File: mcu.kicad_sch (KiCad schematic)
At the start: 38 parts, among them J3 Conn_ST_STDC14, J4 USB_5V, J5 E5V, SW2 BOOT0 pull, U1 STM32G474RETx, U2 AMS1117-3.3, Y1 Crystal 32.768KHz, Y2 Crystal 24MHz

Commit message: Added finishing thouches to brake sense pcb Finished main schematic layout and added chosen component footprints Placed components in layout and started tracing
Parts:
- removed C43, C50: 100nF, Capacitor_SMD:C_0603_1608Metric_Pad1.08x0.95mm_HandSolder, symbol Device:C
- removed J4: USB_5V, Project_Footprints:HARWIN_M20-9990246, symbol M20-9990246:M20-9990246
- removed J5: E5V, Project_Footprints:HARWIN_M20-9990246, symbol M20-9990246:M20-9990246
- removed R27: 47, Resistor_SMD:R_0805_2012Metric_Pad1.20x1.40mm_HandSolder, symbol Device:R
- removed U2: AMS1117-3.3, Package_TO_SOT_SMD:SOT-223-3_TabPin2, symbol Regulator_Linear:AMS1117-3.3
- added C31, C33: 100nF, Capacitor_SMD:C_0603_1608Metric, symbol Device:C
- added C32: 1μF, Capacitor_SMD:C_0603_1608Metric, symbol Device:C
- added D4: APT2012CGCK, LED_SMD:LED_0805_2012Metric, symbol Device:LED
- added D5, D6: SS34, Diode_SMD:D_SOD-323, symbol Device:D_Zener
- added FB2: 600R@100MHz, Inductor_SMD:L_0603_1608Metric, symbol Device:FerriteBead
- added J3: USB_5V, tinynav:HARWIN_M20-9990246, symbol tinynav:M20-9990246
- added J4: E5V, tinynav:HARWIN_M20-9990246, symbol tinynav:M20-9990246
- added J5: Curr_measure, tinynav:HARWIN_M20-9990246, symbol tinynav:M20-9990246
- added R13: 560, Resistor_SMD:R_0805_2012Metric, symbol Device:R
- added U5: TLV75533PDBV, Package_TO_SOT_SMD:SOT-23-5, symbol Regulator_Linear:TLV75533PDBV
- C12: renamed from C8; value 22u -> 1μF; footprint Capacitor_SMD:C_0805_2012Metric -> Capacitor_SMD:C_0603_1608Metric
- C13: renamed from C77; footprint Capacitor_SMD:C_0603_1608Metric_Pad1.08x0.95mm_HandSolder -> Capacitor_SMD:C_0603_1608Metric
- C20: renamed from C40; footprint Capacitor_SMD:C_1206_3216Metric_Pad1.33x1.80mm_HandSolder -> Capacitor_SMD:C_1206_3216Metric
- C21: renamed from C44; footprint Capacitor_SMD:C_0603_1608Metric_Pad1.08x0.95mm_HandSolder -> Capacitor_SMD:C_0603_1608Metric
- C22: renamed from C47; footprint Capacitor_SMD:C_0603_1608Metric_Pad1.08x0.95mm_HandSolder -> Capacitor_SMD:C_0603_1608Metric
- C23: renamed from C48; footprint Capacitor_SMD:C_0603_1608Metric_Pad1.08x0.95mm_HandSolder -> Capacitor_SMD:C_0603_1608Metric
- C24: renamed from C49; footprint Capacitor_SMD:C_0603_1608Metric_Pad1.08x0.95mm_HandSolder -> Capacitor_SMD:C_0603_1608Metric
- C26: renamed from C41; footprint Capacitor_SMD:C_0805_2012Metric_Pad1.18x1.45mm_HandSolder -> Capacitor_SMD:C_0603_1608Metric
- C27: renamed from C45; footprint Capacitor_SMD:C_0603_1608Metric_Pad1.08x0.95mm_HandSolder -> Capacitor_SMD:C_0603_1608Metric
- C28: renamed from C42; footprint Capacitor_SMD:C_0805_2012Metric_Pad1.18x1.45mm_HandSolder -> Capacitor_SMD:C_0603_1608Metric
- C29: renamed from C46; footprint Capacitor_SMD:C_0603_1608Metric_Pad1.08x0.95mm_HandSolder -> Capacitor_SMD:C_0603_1608Metric
- C30: renamed from C76; footprint Capacitor_SMD:C_0603_1608Metric_Pad1.08x0.95mm_HandSolder -> Capacitor_SMD:C_0603_1608Metric
- R10: renamed from R24; footprint Resistor_SMD:R_0805_2012Metric_Pad1.20x1.40mm_HandSolder -> Resistor_SMD:R_0805_2012Metric
- R11: renamed from R25; footprint Resistor_SMD:R_0805_2012Metric_Pad1.20x1.40mm_HandSolder -> Resistor_SMD:R_0805_2012Metric
- R12: renamed from R23; footprint Resistor_SMD:R_0805_2012Metric_Pad1.20x1.40mm_HandSolder -> Resistor_SMD:R_0805_2012Metric
- Y1: renamed from Y2; footprint Crystal:Crystal_SMD_3225-4Pin_3.2x2.5mm -> Crystal:Crystal_SMD_2016-4Pin_2.0x1.6mm
- renumbered C3 to C10, C4 to C11, C5 to C8, C6 to C9, J3 to J2, R2 to R5, R1 to R6, R3 to R7, R4 to R8, R5 to R9, Y1 to Y2
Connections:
- net +3V3: now also U1.1 (VBAT), U1.16 (VDD), U1.32 (VDD), U1.48 (VDD), U1.64 (VDD), C33.1, FB2.1, J5.1; no longer C12.1, C26.1, C27.1, C28.1, C29.1
- net E5V: now also J4.2
- net GND: now also C12.2, R7.2, C31.2, C32.2, C33.2, D4.1 (K), U5.2 (GND)
- net USB/USB_5V: now also J3.2
- net SWDIO: now reaches R10.2, U1.49 (PA13)
- net HSE_OUT: now reaches C9.2, U1.6 (PF1), Y1.3
- net NRST: now reaches C13.1, D11.1 (K), J2.12 (~{RST}), RESET1.1 (A), U1.7 (PG10)
- net LSE_IN: now reaches R6.2, U1.3 (PC14)
- net HSE_IN: now reaches R5.2, U1.5 (PF0)
- net LSE_OUT: now reaches C11.2, U1.4 (PC15), Y2.2
- net BOOT: now reaches R12.1, U1.61 (PB8)
- net SWCLK: now reaches R11.2, U1.50 (PA14)
- new net: D4.2 (A), R13.2
- new net: D6.2 (A), J4.1
- new net: D5.2 (A), J3.1
- new net +5V: C31.1, C32.1, D5.1 (K), D6.1 (K), R13.1, U5.1 (IN), U5.3 (EN)
- new net 3.3V_OUT: C12.1, J5.2, U5.5 (OUT)
- new net VDDA: C26.1, C27.1, C28.1, C29.1, FB2.2, U1.28 (VREF+), U1.29 (VDDA)
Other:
- note added: "Don't need both mechanical (jumper) and diode protection Using both to test if one work better"
- note added: "VDDA/ VREF+"
- note removed: "BOOT"
- note removed: "NRST"
- note removed: "VDDA"
- moved on the sheet: C12, C13, C20, C21, C22, C23, C24, C26, C27, C28, C29, C30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

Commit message: Added Current reading for INA228 Started rev 02 on brake sense
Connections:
- net +3V3: now also R8.2, R9.2
- net GND: no longer R8.2, R9.2
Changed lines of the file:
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@@
 	)
 	(junction
+		(at 92.71 152.4)
+		(diameter 0)
+		(color 0 0 0 0)
+	)
+	(junction
 		(at 54.61 179.07)
 		(diameter 0)
@@
 	)
 	(junction
-		(at 92.71 152.4)
-		(diameter 0)
-		(color 0 0 0 0)
-	)
-	(junction
 		(at 262.89 130.81)
 		(diameter 0)
@@
 	(wire
 		(pts
-			(xy 92.71 152.4) (xy 96.52 152.4)
+			(xy 88.9 152.4) (xy 92.71 152.4)
 		)
 		(stroke
@@
 	(wire
 		(pts
-			(xy 88.9 152.4) (xy 92.71 152.4)
-		)
-		(stroke
-			(width 0)
-			(type default)
-		)
-	)
-	(wire
-		(pts
 			(xy 78.74 50.8) (xy 78.74 49.53)
 		)
@@
 	(wire
 		(pts
+			(xy 92.71 152.4) (xy 96.52 152.4)
+		)
+		(stroke
+			(width 0)
+			(type default)
+		)
+	)
+	(wire
+		(pts
 			(xy 90.17 33.02) (xy 90.17 38.1)
 		)
@@
 	)
 	(symbol
+		(lib_id "power:+3V3")
+		(at 92.71 152.4 180)
+		(unit 1)
+		(body_style 1)
+		(exclude_from_sim no)
+		(in_bom yes)
+		(on_board yes)
+		(in_pos_files yes)
+		(dnp no)
+		(fields_autoplaced yes)
+		(property "Reference" "#PWR058"
+			(at 92.71 148.59 0)
+			(hide yes)
+			(show_name no)
+			(do_not_autoplace no)
+			(effects
+				(font
+					(size 1.27 1.27)
+				)
+			)
+		)
+		(property "Value" "+3V3"
+			(at 92.71 157.48 0)
+			(show_name no)
+			(do_not_autoplace no)
+			(effects
+				(font
+					(size 1.27 1.27)
+				)
+			)
+		)
+		(property "Footprint" ""
+			(at 92.71 152.4 0)
+			(hide yes)
+			(show_name no)
+			(do_not_autoplace no)
+			(effects
+				(font
+					(size 1.27 1.27)
+				)
+			)
+		)
+		(property "Datasheet" ""
+			(at 92.71 152.4 0)
+			(hide yes)
+			(show_name no)
+			(do_not_autoplace no)
+			(effects
+				(font
+					(size 1.27 1.27)
+				)
+			)
+		)
+		(property "Description" "Power symbol creates a global label with name \"+3V3\""
+			(at 92.71 152.4 0)
+			(hide yes)
+			(show_name no)
+			(do_not_autoplace no)
+			(effects
+				(font
+					(size 1.27 1.27)
+				)
+			)
+		)
+		(pin "1"
+		)
+		(instances
+			(project "Nucleo_devboard"
+				(path "/4250c3cc-f8c5-441a-9e80-e89bb6ada756/77213db3-d061-4eb8-a107-9e1bca2752d0"
+					(reference "#PWR058")
+					(unit 1)
+				)
+			)
+		)
+	)
+	(symbol
 		(lib_id "tinynav:M20-9990246")
 		(at 44.45 52.07 270)
@@
 					(unit 1)
 				)
-			)
-		)
-	)
-	(symbol
-		(lib_id "power:GND")
-		(at 92.71 152.4 0)
-		(unit 1)
-		(body_style 1)
-		(exclude_from_sim no)
-		(in_bom yes)
-		(on_board yes)
-		(in_pos_files yes)
-		(dnp no)
-		(fields_autoplaced yes)
-		(property "Reference" "#PWR06"
-			(at 92.71 158.75 0)
-			(hide yes)
-			(show_name no)
-			(do_not_autoplace no)
-			(effects
-				(font
-					(size 1.27 1.27)
-				)
-			)
-		)
-		(property "Value" "GND"
-			(at 92.71 157.48 0)
-			(show_name no)
-			(do_not_autoplace no)
-			(effects
-				(font
-					(size 1.27 1.27)
-				)
-			)
-		)
-		(property "Footprint" ""
-			(at 92.71 152.4 0)
-			(hide yes)
-			(show_name no)
-			(do_not_autoplace no)
-			(effects
-				(font
-					(size 1.27 1.27)
-				)
-			)
-		)
-		(property "Datasheet" ""
-			(at 92.71 152.4 0)
-			(hide yes)
-			(show_name no)
-			(do_not_autoplace no)
-			(effects
-				(font
-					(size 1.27 1.27)
-				)
-			)
-		)
-		(property "Description" "Power symbol creates a global label with name \"GND\" , ground"
-			(at 92.71 152.4 0)
-			(hide yes)
-			(show_name no)
-			(do_not_autoplace no)
-			(effects
-				(font
-					(size 1.27 1.27)
-				)
-			)
-		)
-		(pin "1"
-		)
-		(instances
-			(project "Nucleo_devboard"
-				(path "/4250c3cc-f8c5-441a-9e80-e89bb6ada756/77213db3-d061-4eb8-a107-9e1bca2752d0"
-					(reference "#PWR06")
-					(unit 1)
-				)

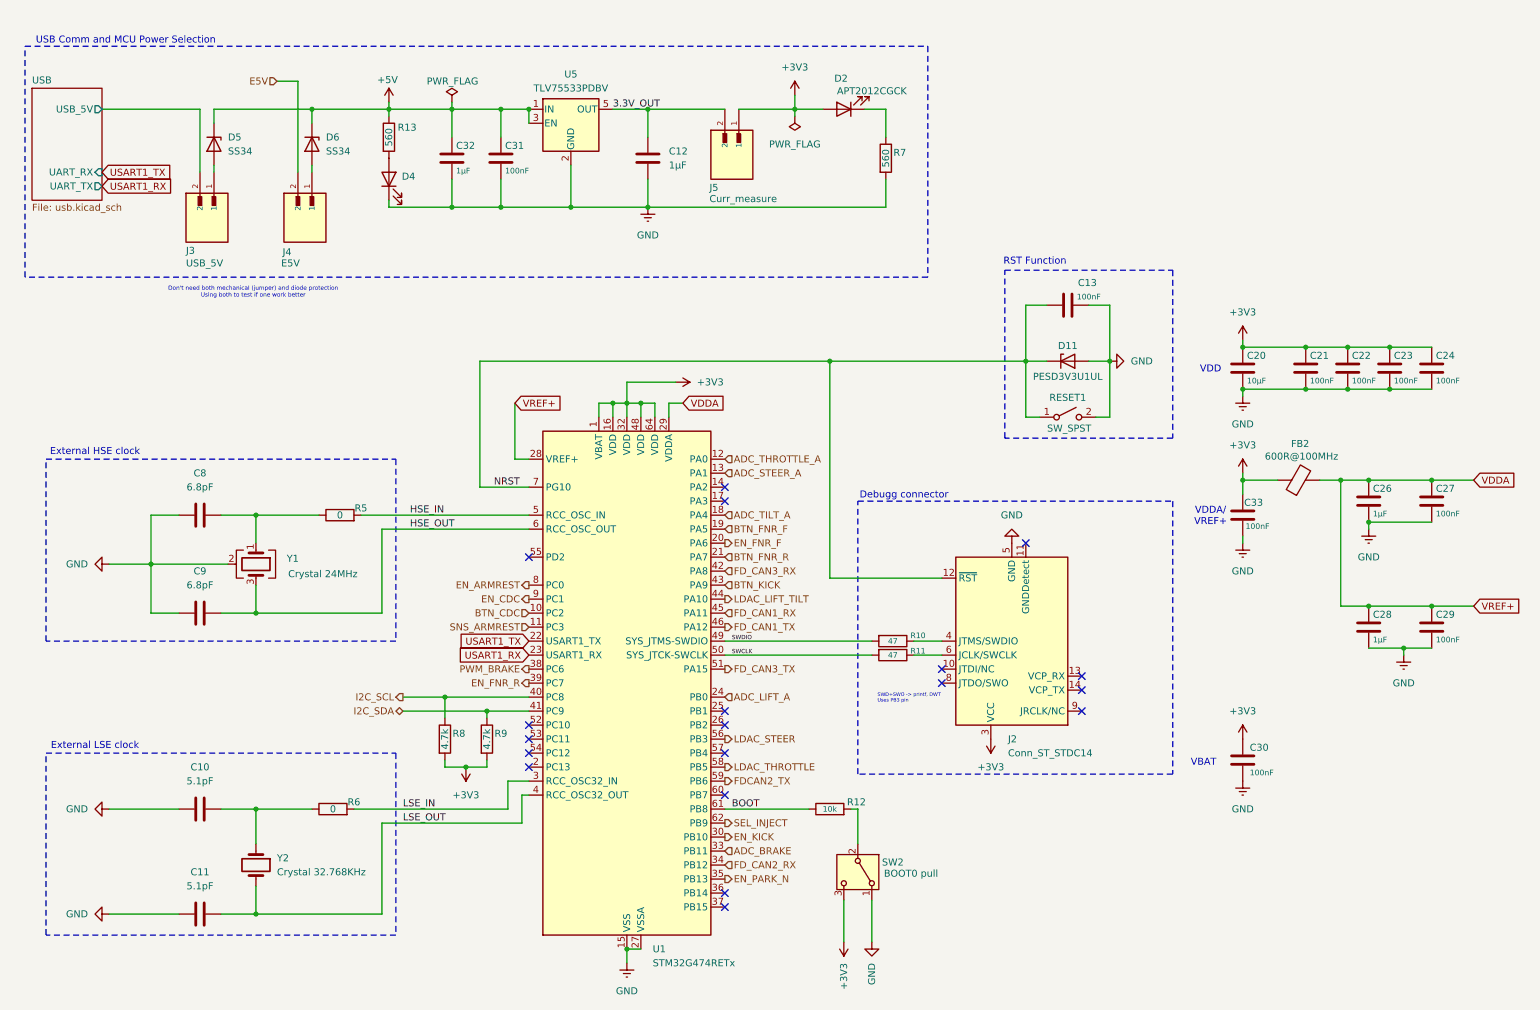
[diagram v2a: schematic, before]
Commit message: added rev04_mcu1/2.h revised brake sense board Added logic for 2 MCUs on nucleo board
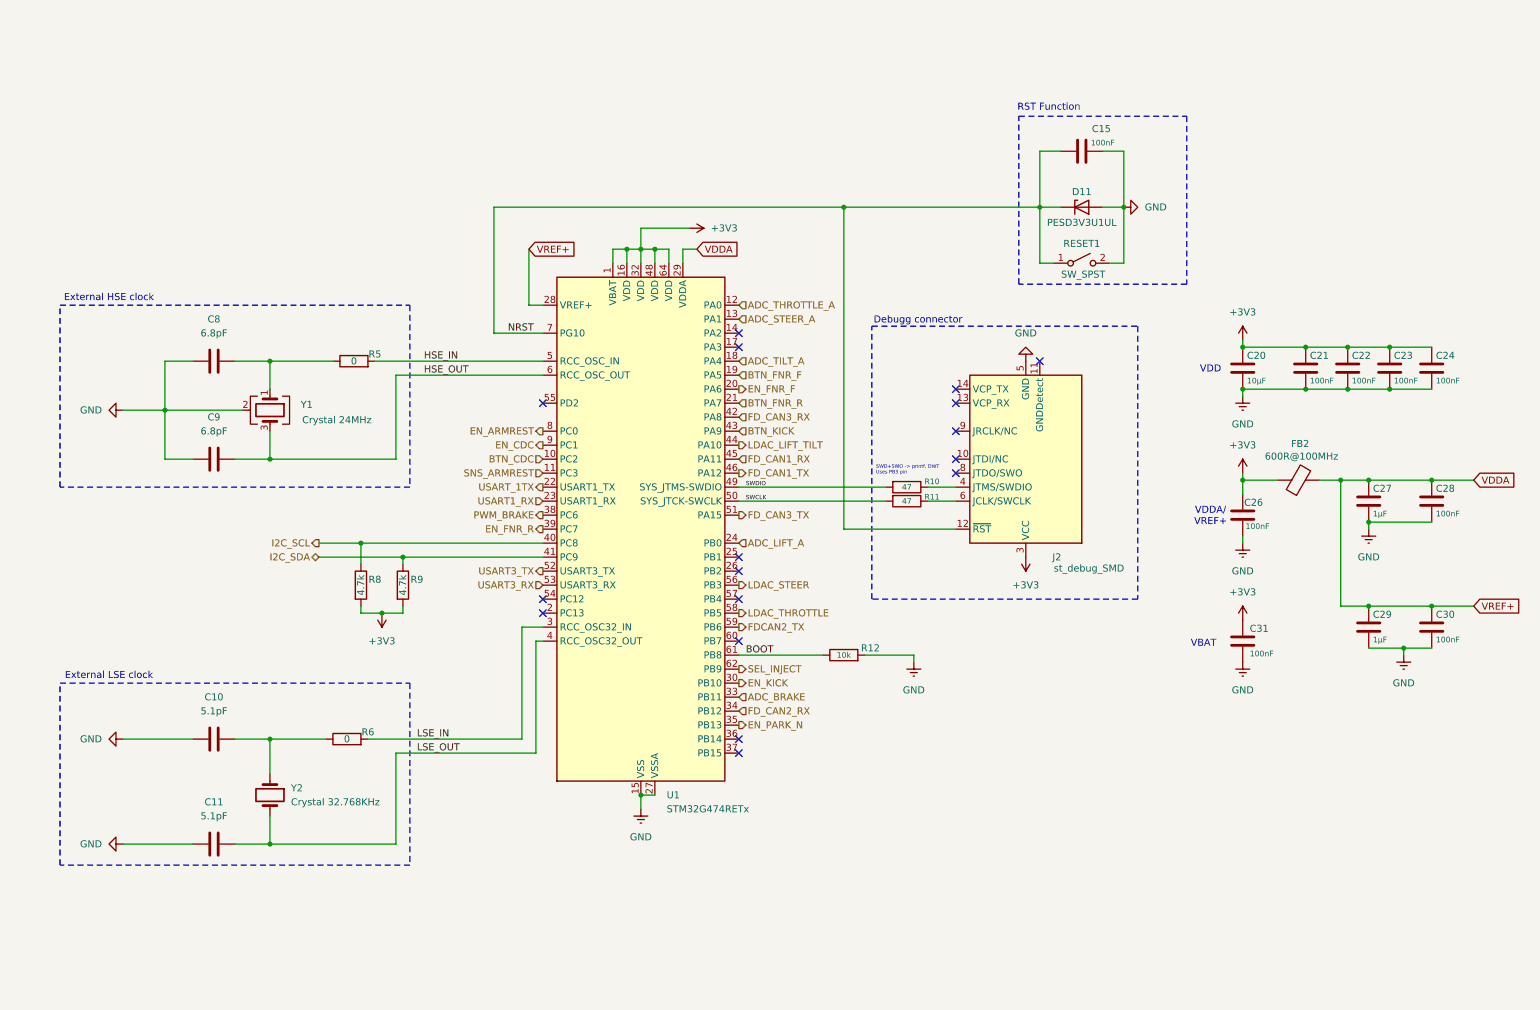
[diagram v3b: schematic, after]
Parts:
- removed C12, C32: 1μF, Capacitor_SMD:C_0603_1608Metric, symbol Device:C
- removed C31: 100nF, Capacitor_SMD:C_0603_1608Metric, symbol Device:C
- removed D2, D4: APT2012CGCK, LED_SMD:LED_0805_2012Metric, symbol Device:LED
- removed D5, D6: SS34, Diode_SMD:D_SOD-323, symbol Device:D_Zener
- removed J2: Conn_ST_STDC14, Connector_PinHeader_1.27mm:PinHeader_2x07_P1.27mm_Vertical, symbol Connector:Conn_ST_STDC14
- removed J3: USB_5V, tinynav:HARWIN_M20-9990246, symbol tinynav:M20-9990246
- removed J4: E5V, tinynav:HARWIN_M20-9990246, symbol tinynav:M20-9990246
- removed J5: Curr_measure, tinynav:HARWIN_M20-9990246, symbol tinynav:M20-9990246
- removed R13, R7: 560, Resistor_SMD:R_0805_2012Metric, symbol Device:R
- removed SW2: BOOT0 pull, Button_Switch_THT:SW_Slide_SPDT_Straight_CK_OS102011MS2Q, symbol Switch:SW_SPDT
- removed U5: TLV75533PDBV, Package_TO_SOT_SMD:SOT-23-5, symbol Regulator_Linear:TLV75533PDBV
- added J2: st_debug_SMD, tinynav:PinHeader_2x07_P1.27mm_Vertical_SMD, symbol tinynav:st_debug_SMD
- renumbered C13 to C15, C33 to C26, C26 to C27, C27 to C28, C28 to C29, C29 to C30, C30 to C31
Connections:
- net +3V3: now also J2.3 (VCC)
- net GND: now also R12.2, J2.5 (GND), J2.7 (GND)
- net NRST: now also J2.12 (~{RST})
- net at R10.1: now also J2.4 (JTMS/SWDIO)
- net at R11.1: now also J2.6 (JCLK/SWCLK)
- net USART3_TX: now reaches U1.52 (PC10)
- net USART3_RX: now reaches U1.53 (PC11)
- net USART1_TX renamed USART_1TX
- no-connect marks 19 -> 17
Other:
- removed sheet USB
- note removed: "Don't need both mechanical (jumper) and diode protection Using both to test if one work better"
- note removed: "USB Comm and MCU Power Selection"
- moved on the sheet: C10, C11, C15, C31, C8, C9, D11, R10, R11, R12, R5, R6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

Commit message: Generated scaffold for mcu2 finished brake sense rev2 finished adding second chip to nucleo devboard
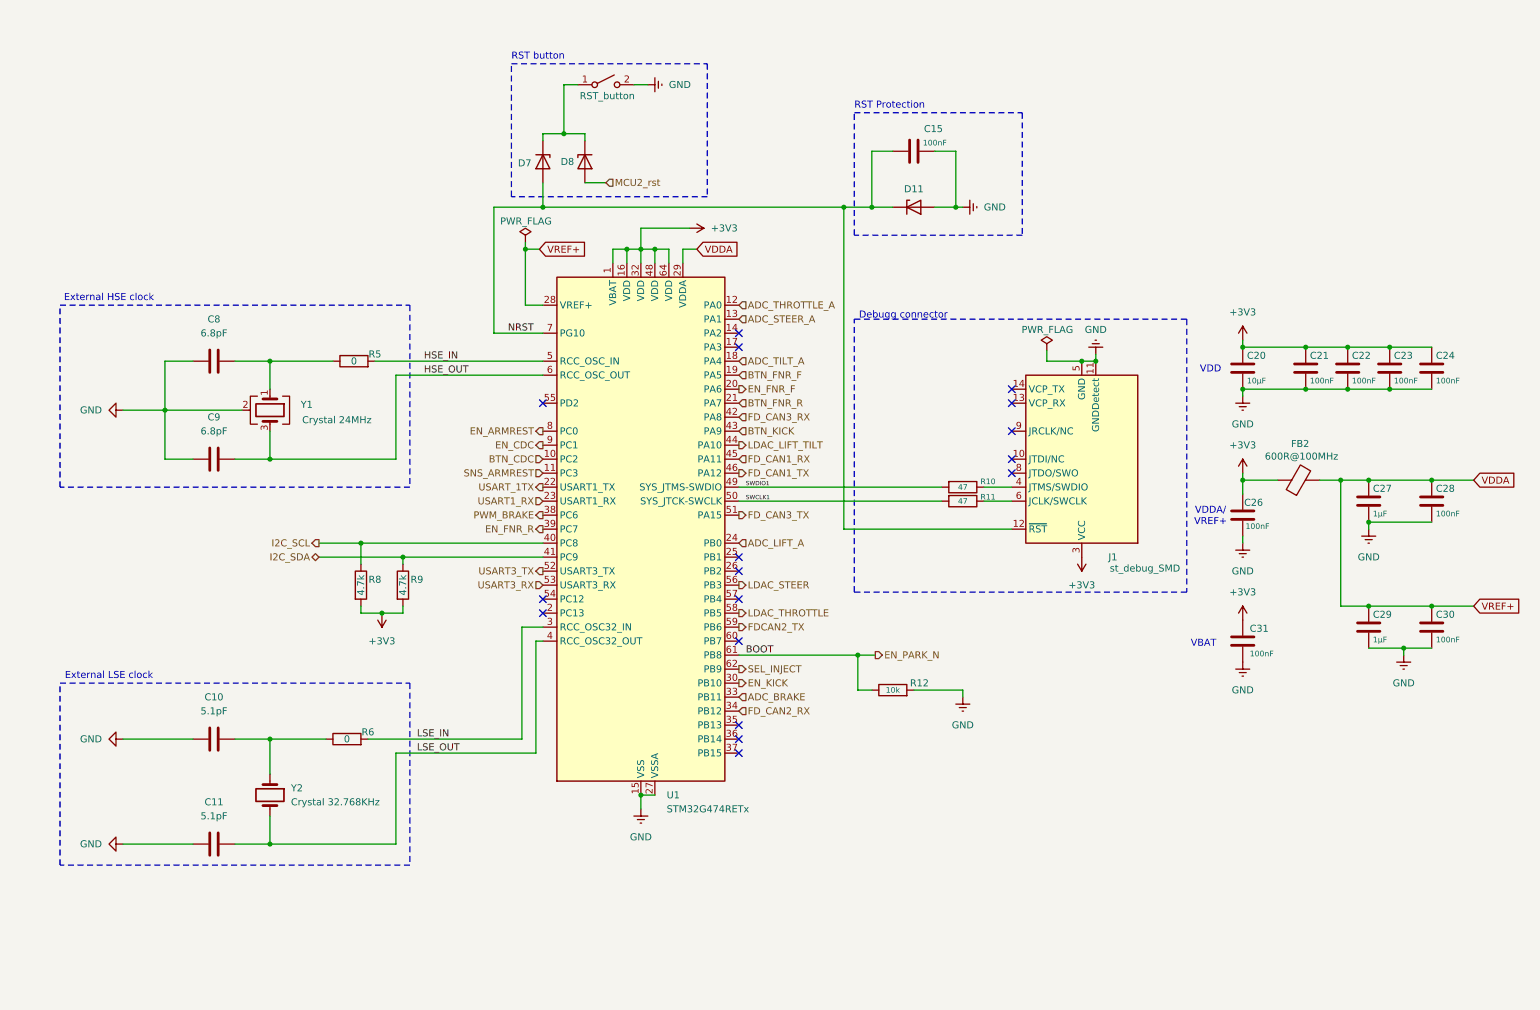
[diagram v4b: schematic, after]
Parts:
- added D7, D8: BAT60A, Diode_SMD:D_SOD-323, symbol Device:D_Zener
- D11: value PESD3V3U1UL -> CDSOD323-T03; footprint Diode_SMD:D_SOD-882 -> Diode_SMD:D_SOD-323
- RESET1: value SW_SPST -> RST_button
- renumbered J2 to J1
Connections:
- net BOOT is gone; now on net EN_PARK_N: R12.1, U1.61 (PB8)
- net EN_PARK_N: no longer U1.35 (PB13)
- net GND: now also J1.11 (GNDDetect)
- net NRST: now also D7.2 (A); no longer RESET1.1 (A)
- net SWCLK renamed SWCLK1
- net SWDIO renamed SWDIO1
- new net: D7.1 (K), D8.1 (K), RESET1.1 (A)
- new net MCU2_rst: D8.2 (A)
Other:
- note added: "RST Protection"
- note added: "RST button"
- note removed: "RST Function"
- note removed: "SWD+SWO -> printf, DWT Uses PB3 pin"
- moved on the sheet: C15, D11, J1, R10, R11, R12

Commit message: Finished last thouches on brake sense and nucleo pcb (Ordered pcbs)
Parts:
- removed D11: CDSOD323-T03, Diode_SMD:D_SOD-323, symbol Diode:PESD3V3U1UL
- added D11: STS321033B401, Diode_SMD:D_SOD-323, symbol Device:D_TVS
- added D8: APT2012CGCK, LED_SMD:LED_0805_2012Metric, symbol Device:LED
- added R19: 560, Resistor_SMD:R_0805_2012Metric, symbol Device:R
- R10, R11: footprint Resistor_SMD:R_0805_2012Metric -> Resistor_SMD:R_0603_1608Metric
- renumbered D7 to D6, D8 to D7
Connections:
- net GND: now also D11.2 (A2), R19.1
- net NRST: now also D11.1 (A1)
- net at U1.35 (PB13): now also D8.2 (A)
- new net: D8.1 (K), R19.2
- no-connect marks 17 -> 16
